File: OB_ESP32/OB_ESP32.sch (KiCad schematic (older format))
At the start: 6 parts

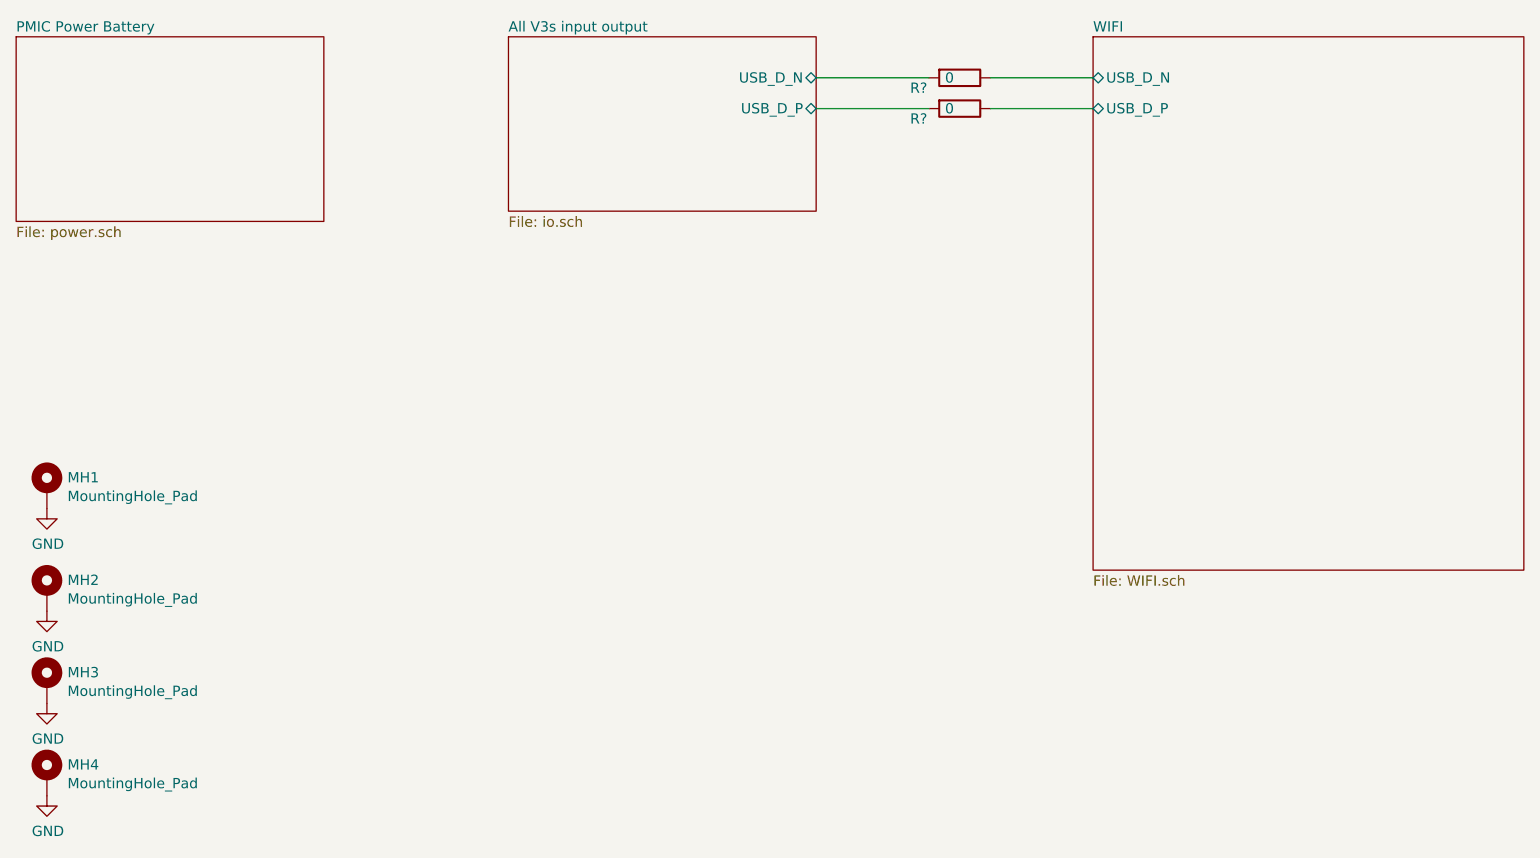
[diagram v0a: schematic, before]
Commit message: +esp32picod4 +fix mounting hole position -ceramic antenna +ufl -spi flash
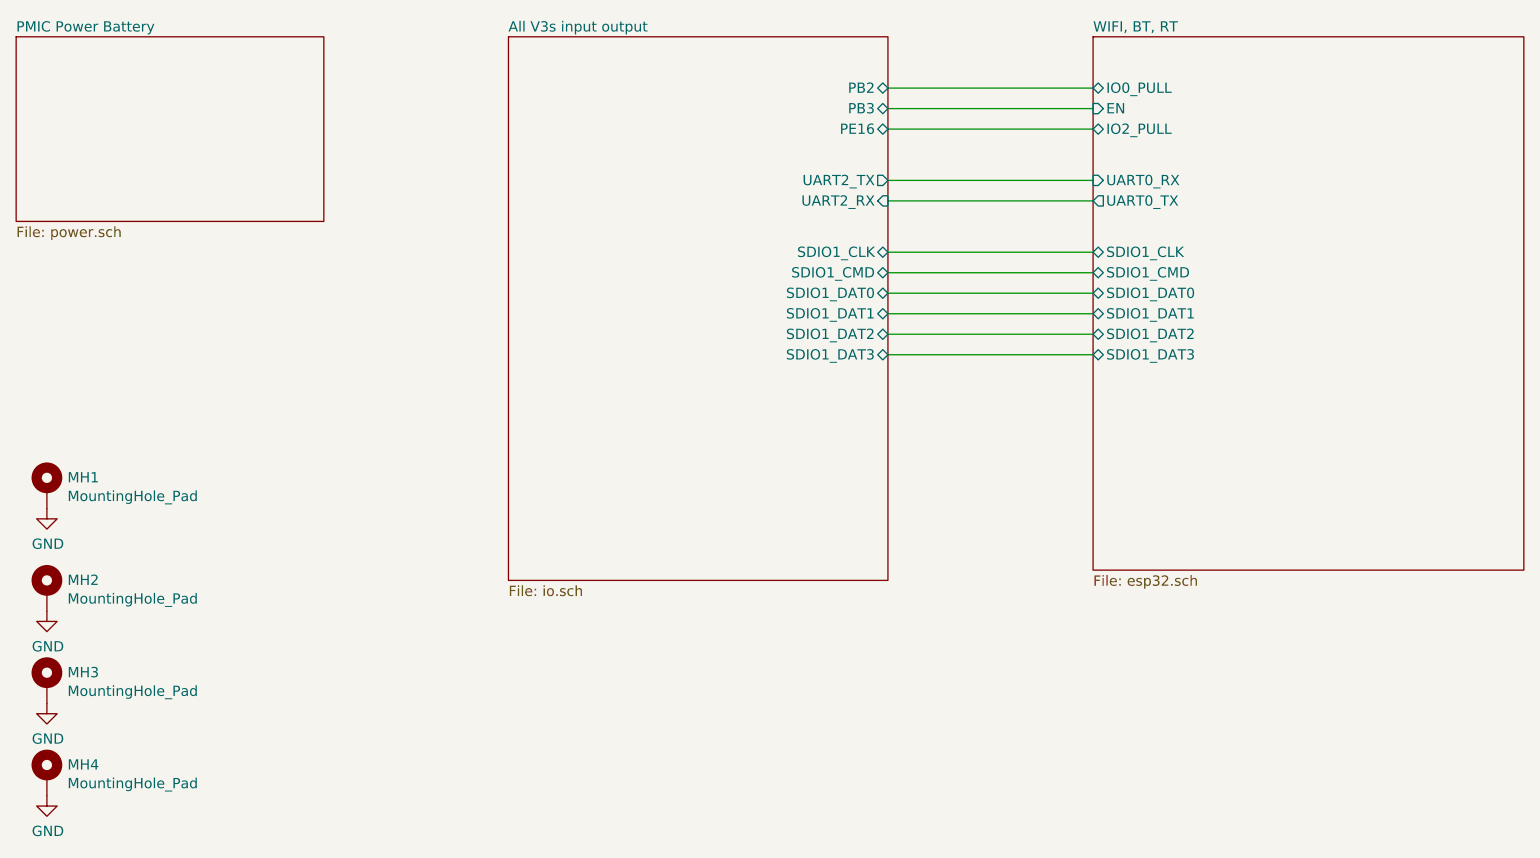
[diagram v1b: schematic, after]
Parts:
- removed R? (x2): 0, Resistor_SMD:R_0402_1005Metric, symbol Device:R
- MH1, MH2, MH3, MH4: footprint MountingHole:MountingHole_3.2mm_M3_ISO14580_Pad -> MountingHole:MountingHole_2.2mm_M2_ISO7380_Pad
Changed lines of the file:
@@
 EESchema Schematic File Version 4
-LIBS:OB-cache
+LIBS:OB_ESP32-cache
 EELAYER 29 0
 EELAYER END
@@
 F1 "power.sch" 50
 $EndSheet
-$Sheet
-S 3650 1300 1500 850
-U 5BC231CE
-F0 "All V3s input output" 50
-F1 "io.sch" 50
-F2 "USB_D_N" B R 5150 1500 50
-F3 "USB_D_P" B R 5150 1650 50
-$EndSheet
 $Comp
 L Mechanical:MountingHole_Pad MH1
@@
 F 0 "MH1" H 1500 3551 50  0000 L CNN
 F 1 "MountingHole_Pad" H 1500 3460 50  0000 L CNN
-F 2 "MountingHole:MountingHole_3.2mm_M3_ISO14580_Pad" H 1400 3500 50  0001 C CNN
+F 2 "MountingHole:MountingHole_2.2mm_M2_ISO7380_Pad" H 1400 3500 50  0001 C CNN
 F 3 "~" H 1400 3500 50  0001 C CNN
 	1    1400 3500
@@
 F 0 "MH2" H 1500 4051 50  0000 L CNN
 F 1 "MountingHole_Pad" H 1500 3960 50  0000 L CNN
-F 2 "MountingHole:MountingHole_3.2mm_M3_ISO14580_Pad" H 1400 4000 50  0001 C CNN
+F 2 "MountingHole:MountingHole_2.2mm_M2_ISO7380_Pad" H 1400 4000 50  0001 C CNN
 F 3 "~" H 1400 4000 50  0001 C CNN
 	1    1400 4000
@@
 F 0 "MH3" H 1500 4501 50  0000 L CNN
 F 1 "MountingHole_Pad" H 1500 4410 50  0000 L CNN
-F 2 "MountingHole:MountingHole_3.2mm_M3_ISO14580_Pad" H 1400 4450 50  0001 C CNN
+F 2 "MountingHole:MountingHole_2.2mm_M2_ISO7380_Pad" H 1400 4450 50  0001 C CNN
 F 3 "~" H 1400 4450 50  0001 C CNN
 	1    1400 4450
@@
 F 0 "MH4" H 1500 4951 50  0000 L CNN
 F 1 "MountingHole_Pad" H 1500 4860 50  0000 L CNN
-F 2 "MountingHole:MountingHole_3.2mm_M3_ISO14580_Pad" H 1400 4900 50  0001 C CNN
+F 2 "MountingHole:MountingHole_2.2mm_M2_ISO7380_Pad" H 1400 4900 50  0001 C CNN
 F 3 "~" H 1400 4900 50  0001 C CNN
 	1    1400 4900
@@
 S 6500 1300 2100 2600
 U 5C7A02C5
-F0 "WIFI" 50
-F1 "WIFI.sch" 50
-F2 "USB_D_P" B L 6500 1650 50
-F3 "USB_D_N" B L 6500 1500 50
+F0 "WIFI, BT, RT" 50
+F1 "esp32.sch" 50
+F2 "EN" I L 6500 1650 50
+F3 "UART0_RX" I L 6500 2000 50
+F4 "UART0_TX" O L 6500 2100 50
+F5 "SDIO1_CLK" B L 6500 2350 50
+F6 "SDIO1_CMD" B L 6500 2450 50
+F7 "SDIO1_DAT1" B L 6500 2650 50
+F8 "SDIO1_DAT2" B L 6500 2750 50
+F9 "SDIO1_DAT3" B L 6500 2850 50
+F10 "IO2_PULL" B L 6500 1750 50
+F11 "SDIO1_DAT0" B L 6500 2550 50
+F12 "IO0_PULL" B L 6500 1550 50
 $EndSheet
-$Comp
-L Device:R R?
-U 1 1 5CA6D3D1
-P 5850 1500
-AR Path="/5C7A02C5/5CA6D3D1" Ref="R?"  Part="1"
-AR Path="/5CA6D3D1" Ref="R?"  Part="1"
-F 0 "R?" V 5900 1300 50  0000 C CNN
-F 1 "0" V 5850 1450 50  0000 C CNN
-F 2 "Resistor_SMD:R_0402_1005Metric" V 5780 1500 50  0001 C CNN
-F 3 "~" H 5850 1500 50  0001 C CNN
-	1    5850 1500
-	0    1    1    0
-$EndComp
-$Comp
-L Device:R R?
-U 1 1 5CA6D3D8
-P 5850 1650
-AR Path="/5C7A02C5/5CA6D3D8" Ref="R?"  Part="1"
-AR Path="/5CA6D3D8" Ref="R?"  Part="1"
-F 0 "R?" V 5900 1450 50  0000 C CNN
-F 1 "0" V 5850 1600 50  0000 C CNN
-F 2 "Resistor_SMD:R_0402_1005Metric" V 5780 1650 50  0001 C CNN
-F 3 "~" H 5850 1650 50  0001 C CNN
-	1    5850 1650
-	0    1    1    0
-$EndComp
+$Sheet
+S 3650 1300 1850 2650
+U 5BC231CE
+F0 "All V3s input output" 50
+F1 "io.sch" 50
+F2 "SDIO1_CLK" B R 5500 2350 50
+F3 "SDIO1_CMD" B R 5500 2450 50
+F4 "SDIO1_DAT1" B R 5500 2650 50
+F5 "SDIO1_DAT2" B R 5500 2750 50
+F6 "SDIO1_DAT3" B R 5500 2850 50
+F7 "SDIO1_DAT0" B R 5500 2550 50
+F8 "UART2_TX" O R 5500 2000 50
+F9 "UART2_RX" I R 5500 2100 50
+F10 "PB2" B R 5500 1550 50
+F11 "PB3" B R 5500 1650 50
+F12 "PE16" B R 5500 1750 50
+$EndSheet
 Wire Wire Line
-	6000 1500 6500 1500
+	5500 2350 6500 2350
 Wire Wire Line
-	6500 1650 6000 1650
+	6500 2450 5500 2450
 Wire Wire Line
-	5700 1650 5150 1650
+	5500 2550 6500 2550
 Wire Wire Line
-	5150 1500 5700 1500
+	6500 2650 5500 2650
+Wire Wire Line
+	5500 2750 6500 2750
+Wire Wire Line
+	6500 2850 5500 2850
+Wire Wire Line
+	5500 1550 6500 1550
+Wire Wire Line
+	5500 1650 6500 1650
+Wire Wire Line
+	5500 2000 6500 2000
+Wire Wire Line
+	6500 2100 5500 2100
+Wire Wire Line
+	6500 1750 5500 1750
 $EndSCHEMATC
